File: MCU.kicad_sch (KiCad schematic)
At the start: 23 parts, among them J5 Micro_SD_Card, U4 EFM32GG332, Y1 Crystal_GND23

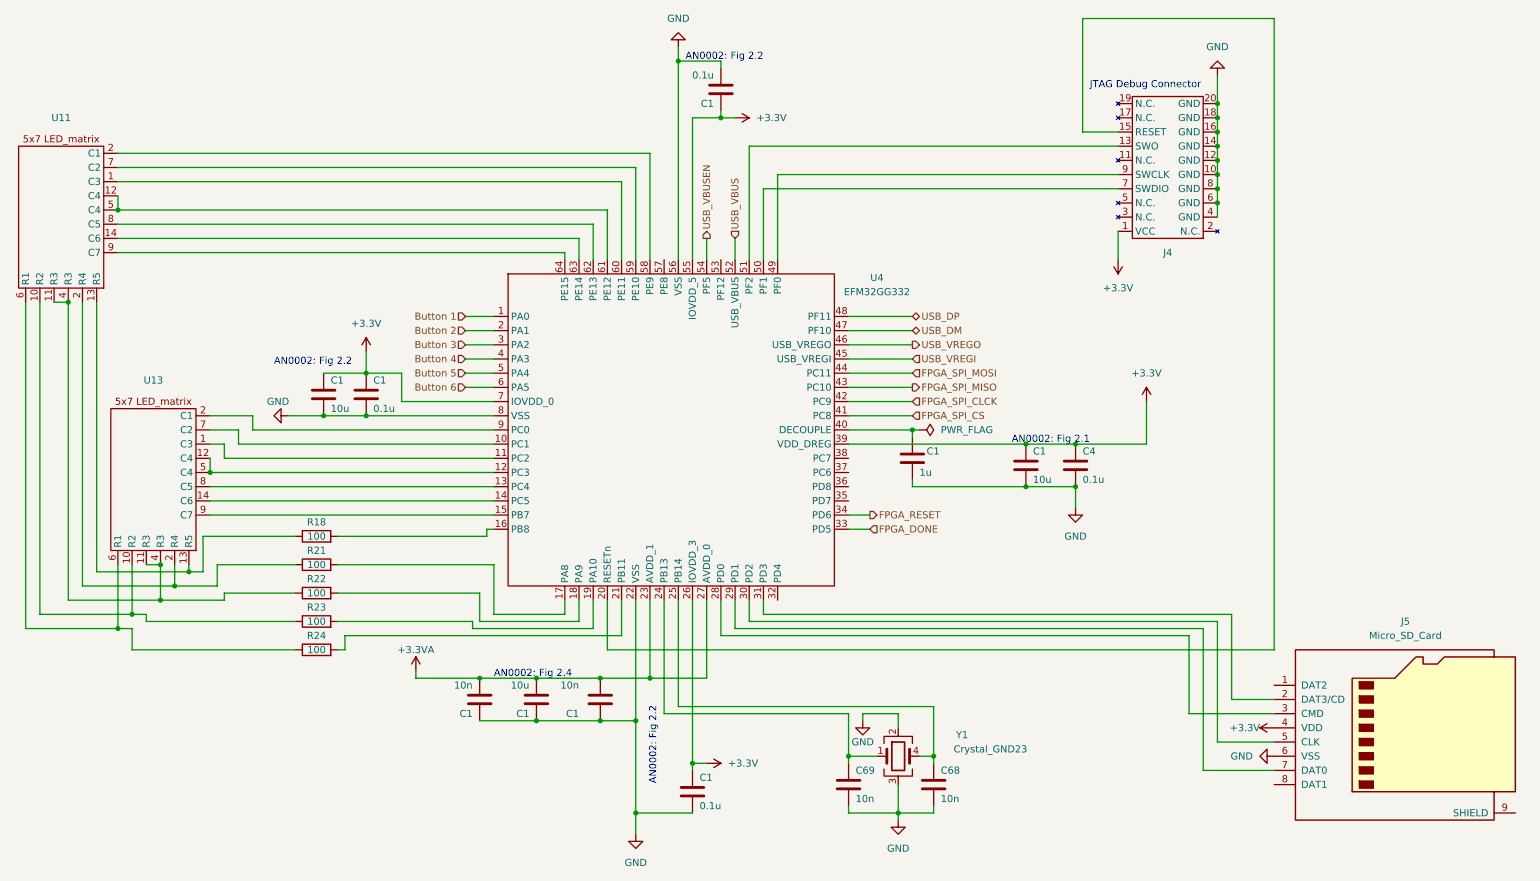
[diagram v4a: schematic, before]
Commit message: Added final GPIO_pins
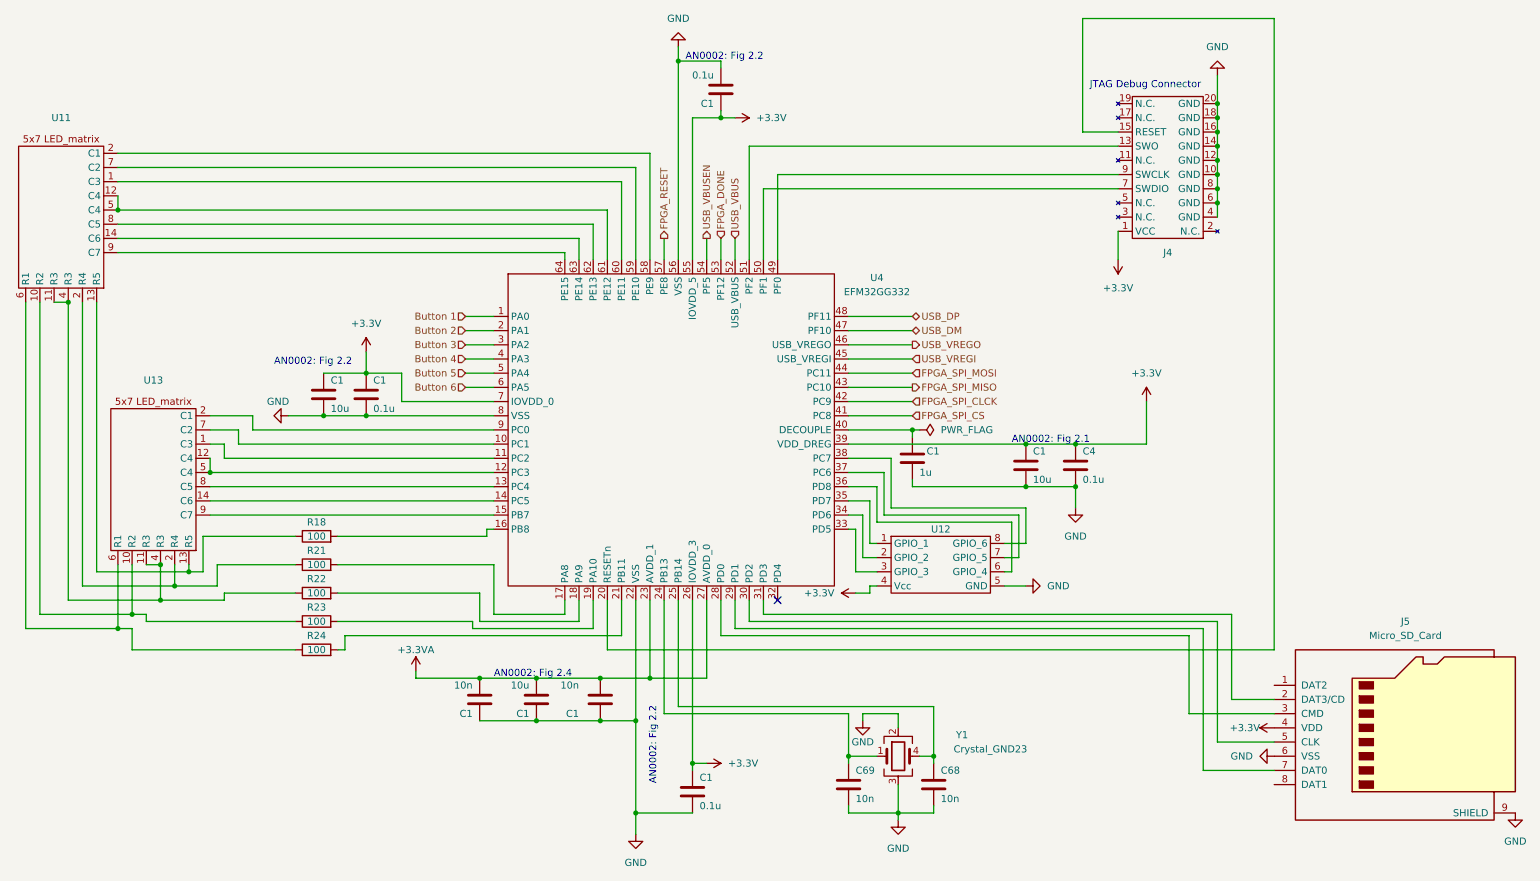
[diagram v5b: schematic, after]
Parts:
- added U12: ~, symbol GuitarZero:MCU_GPIO_Pins
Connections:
- net +3.3V: now also U12.4 (Vcc)
- net FPGA_DONE: now also U4.53 (PF12); no longer U4.33 (PD5)
- net FPGA_RESET: now also U4.57 (PE8); no longer U4.34 (PD6)
- net GND: now also J5.9 (SHIELD), U12.5 (GND)
- net at U4.35 (PD7): now also U12.1 (GPIO_1)
- net at U4.36 (PD8): now also U12.6 (GPIO_4)
- net at U4.37 (PC6): now also U12.7 (GPIO_5)
- net at U4.38 (PC7): now also U12.8 (GPIO_6)
- new net: R21.1, U11.2 (R4), U13.2 (R4)
- new net: U12.3 (GPIO_3), U4.33 (PD5)
- new net: U12.2 (GPIO_2), U4.34 (PD6)
- no-connect marks 0 -> 1

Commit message: Now follows with Electrical Rules
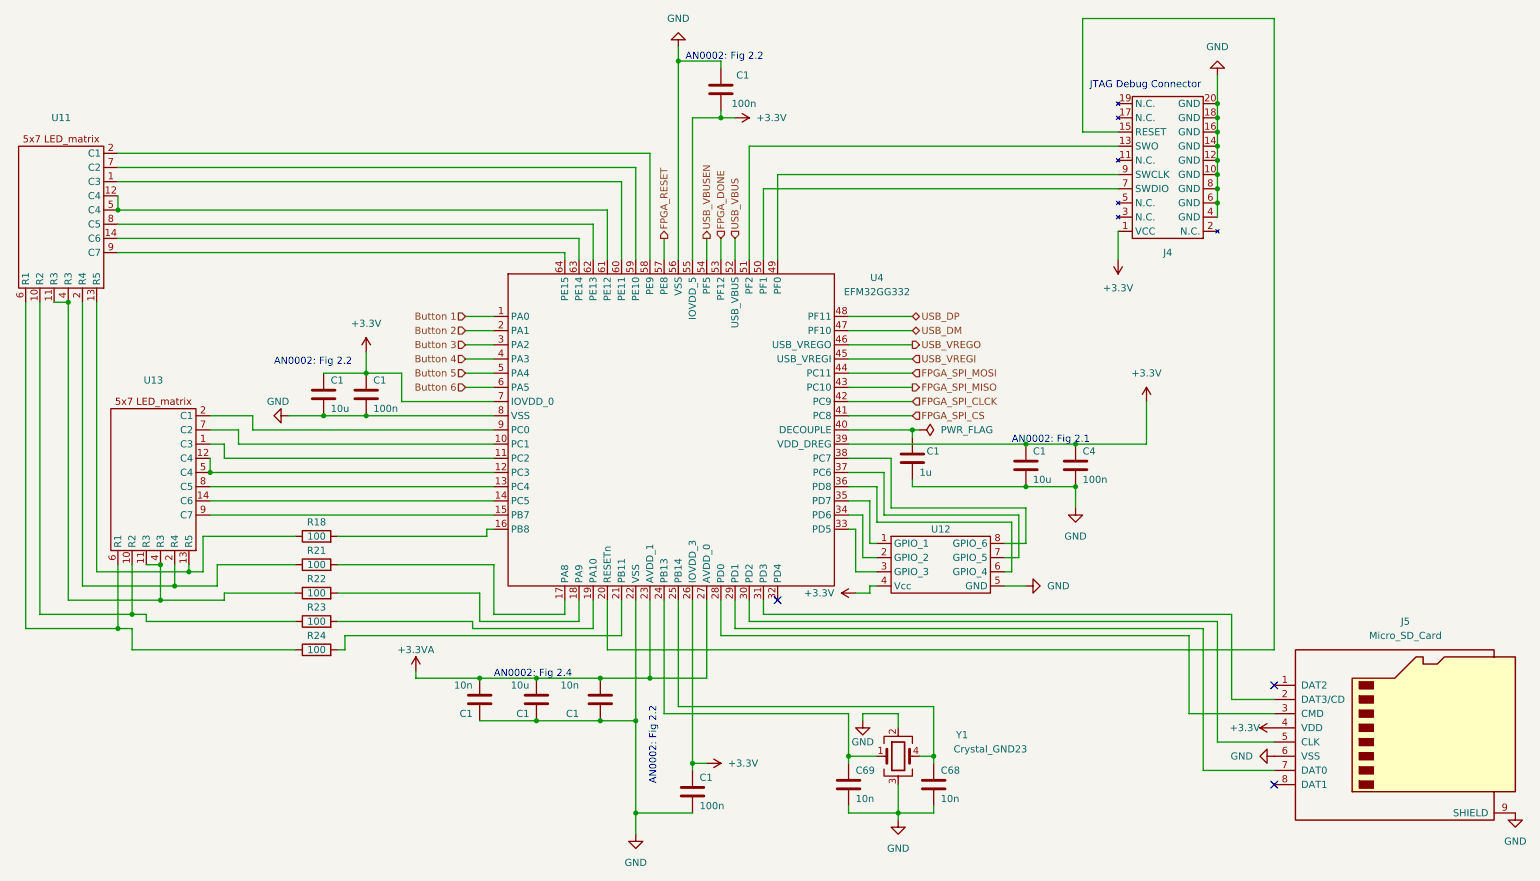
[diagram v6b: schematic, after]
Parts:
- C1, C4: value 0.1u -> 100n
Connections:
- new net: R21.1, U11.2 (R4), U13.2 (R4)
- no-connect marks 1 -> 3

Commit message: Corrected FPGA Debug pin order
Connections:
- new net: R21.1, U11.2 (R4), U13.2 (R4)

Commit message: Added Anti-noise resistors to DAC
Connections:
- new net: R21.1, U11.2 (R4), U13.2 (R4)
